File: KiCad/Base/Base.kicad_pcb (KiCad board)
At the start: 2 copper layers, 100 x 160 mm, 22 parts, among them J1 Raspberry_Pi_2_3_0, J10 MOSFET_output_1, J11 MOSFET_output_2, J12 MOSFET_output_3, J14 Power_switch, J15 VCC, J16 GND, J2 SCL, J3 SDA, J4 12V_Barrel_Jack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

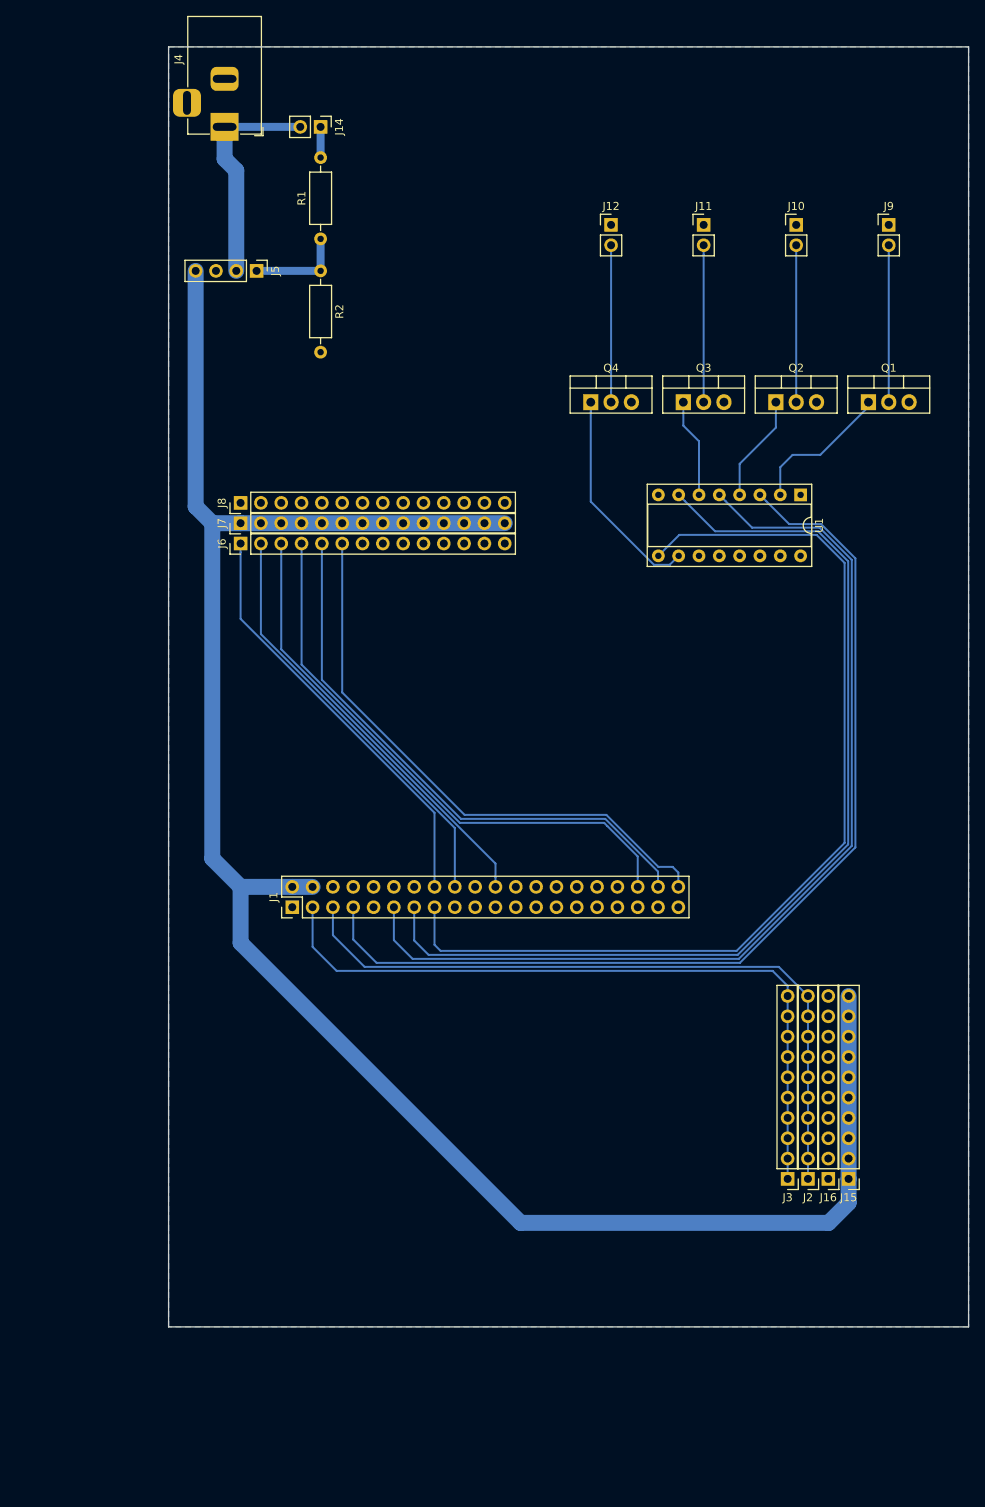
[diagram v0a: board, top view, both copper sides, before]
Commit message: Added pull-down resistors to MOSFET outputs
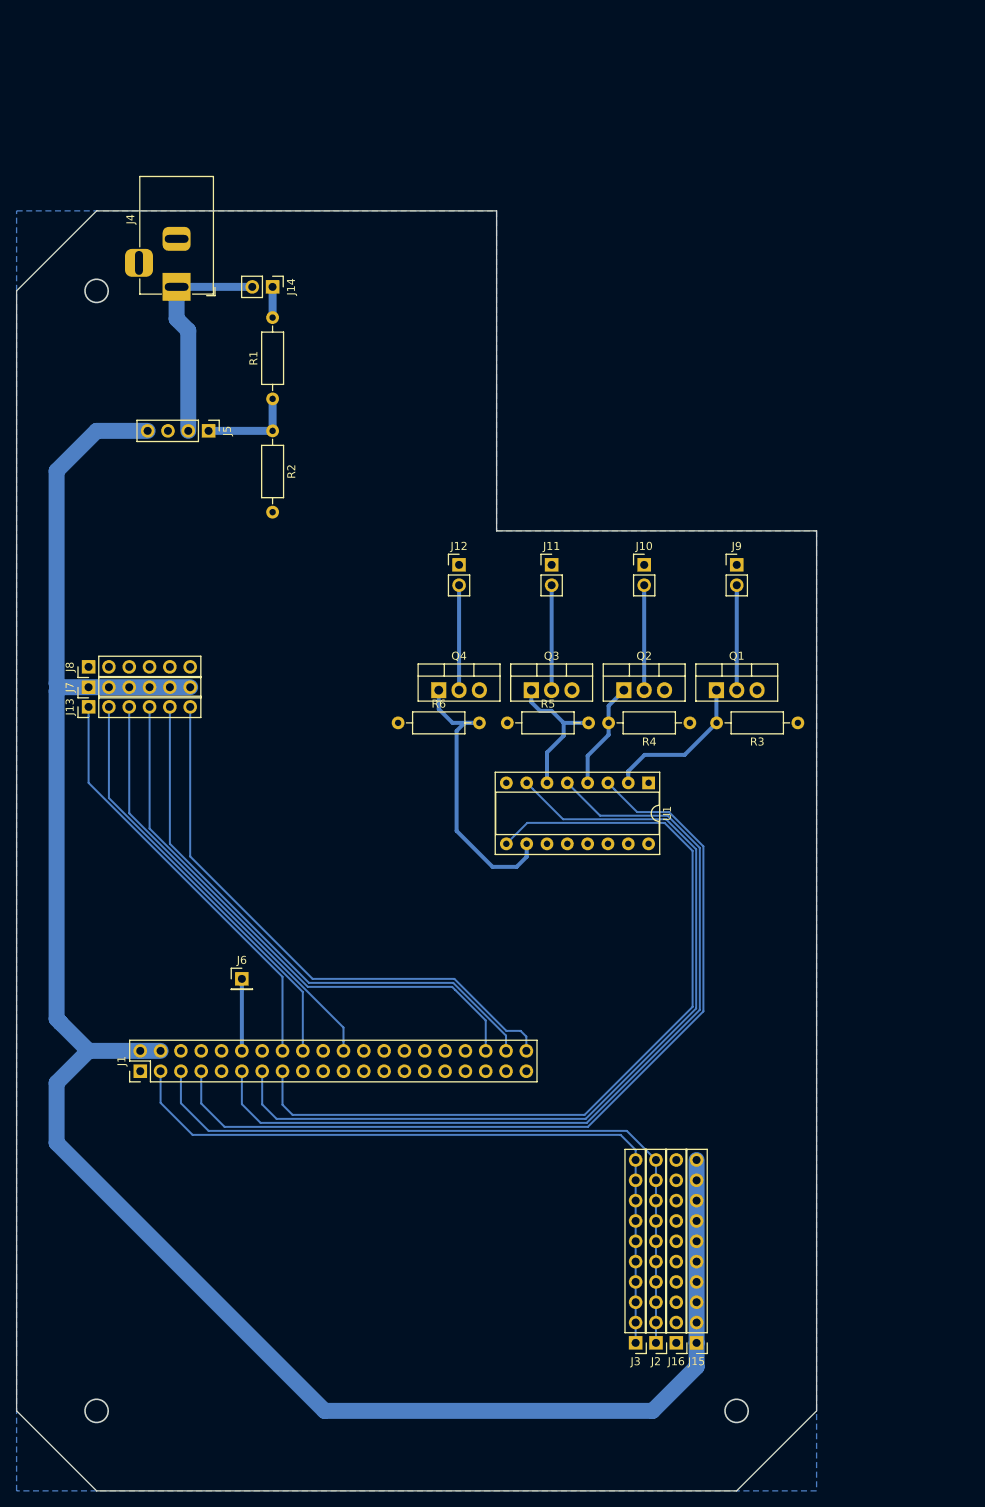
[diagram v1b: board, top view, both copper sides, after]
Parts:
- added J13: GPIO, Connector_PinHeader_2.54mm:PinHeader_1x06_P2.54mm_Vertical, F.Cu at (29.0, 83.5)
- added R3: 10k, Resistor_THT:R_Axial_DIN0207_L6.3mm_D2.5mm_P10.16mm_Horizontal, F.Cu at (117.7, 85.5)
- added R4: 10k, Resistor_THT:R_Axial_DIN0207_L6.3mm_D2.5mm_P10.16mm_Horizontal, F.Cu at (104.2, 85.5)
- added R5: 10k, Resistor_THT:R_Axial_DIN0207_L6.3mm_D2.5mm_P10.16mm_Horizontal, F.Cu at (81.3, 85.5)
- added R6: 10k, Resistor_THT:R_Axial_DIN0207_L6.3mm_D2.5mm_P10.16mm_Horizontal, F.Cu at (67.7, 85.5)
- J5: value Voltage_regulator_board -> VREG
- J6: value GPC_gpio -> PWM; footprint Connector_PinHeader_2.54mm:PinHeader_1x14_P2.54mm_Vertical -> Connector_PinHeader_2.54mm:PinHeader_1x01_P2.54mm_Vertical
- J7: value GPC_VCC -> GPIO; footprint Connector_PinHeader_2.54mm:PinHeader_1x14_P2.54mm_Vertical -> Connector_PinHeader_2.54mm:PinHeader_1x06_P2.54mm_Vertical
- J8: value GPC_GND -> GPIO; footprint Connector_PinHeader_2.54mm:PinHeader_1x14_P2.54mm_Vertical -> Connector_PinHeader_2.54mm:PinHeader_1x06_P2.54mm_Vertical
- moved J6 54.4 mm to (48.2, 117.5), turned to 0 degrees
- moved J9 46.6 mm to (110.0, 65.8)
- moved J10 46.6 mm to (98.5, 65.8)
- moved J11 46.6 mm to (86.9, 65.8)
- moved J12 46.6 mm to (75.3, 65.8)
- moved Q1 40.7 mm to (107.5, 81.4)
- moved Q2 40.7 mm to (95.9, 81.4)
- moved Q3 40.7 mm to (84.3, 81.4)
- moved Q4 40.7 mm to (72.8, 81.4)
- moved U1 40.7 mm to (99.0, 93.0)
- moved J7 28.0 mm to (29.0, 81.0)
- moved J15 28.0 mm to (105.0, 163.0)
- moved J16 28.0 mm to (102.5, 163.0)
- moved J2 28.0 mm to (99.9, 163.0)
- moved J3 28.0 mm to (97.4, 163.0)
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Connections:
- J1 pad 12: (no net) -> /PWM0
- J1 pad 39: (no net) -> GND
- J6 pad 1: /GPC0 -> /PWM0
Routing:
- net /MOUT3: track 122.7 -> 106.9 mm
- net /MOUT2: track 124.9 -> 109.4 mm
- net /MOUT0: track 125.3 -> 109.8 mm
- net /MOUT1: track 123.9 -> 108.4 mm
- net Net-(Q4-Pad1): track 27.2 -> 36.7 mm
- net /PWM0: track 0.00 -> 9.00 mm
- net Net-(J12-Pad2): track 19.6 -> 13.1 mm
- net Net-(J11-Pad2): track 19.6 -> 13.1 mm
- net Net-(J10-Pad2): track 19.6 -> 13.1 mm
- net Net-(J9-Pad2): track 19.6 -> 13.2 mm
- net Net-(Q3-Pad1): track 12.4 -> 18.1 mm
- net Net-(Q1-Pad1): track 18.2 -> 19.1 mm
- net VCC: track 249.3 -> 248.5 mm
- net Net-(J1-Pad3): track 90.5 -> 89.9 mm
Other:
- outline, holes or cut-outs redrawn
- net class 0.5 added: clearance 0.2, trace_width 0.5, via_dia 0.8, via_drill 0.4
- net class Default: trace_width 0.25 -> 0.5
- net class MOSFET_connector added: clearance 0.2, trace_width 2, via_dia 0.8, via_drill 0.4
